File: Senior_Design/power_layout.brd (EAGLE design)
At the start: 108.2 x 35 mm, 103 parts, among them J1 AU-Y1008-2, J1[SIMCARD] 78646-3001, J2 U.FL-R-SMT-1(01), J3 U.FL-R-SMT-1(01), J4[GROVE] 640456-4, T1 BCX70SMD, T2 BCX70SMD, U1 SIM7000E, U2 TUSB2046BVFR, U3 MAX3373EEKA+T, U4 TPS2044BDR, X1 332-04

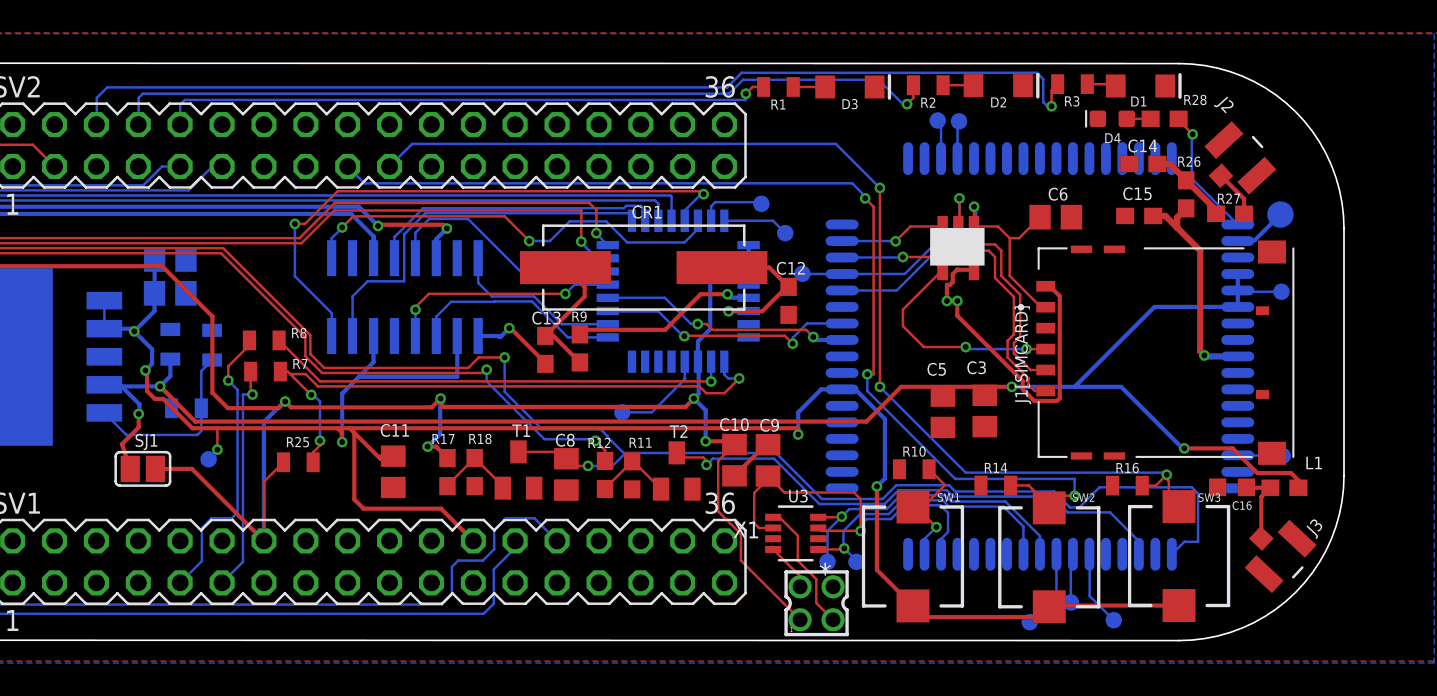
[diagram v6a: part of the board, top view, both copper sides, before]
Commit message: Alpha Order Design Changes
Incorporated all PCB Review design changes
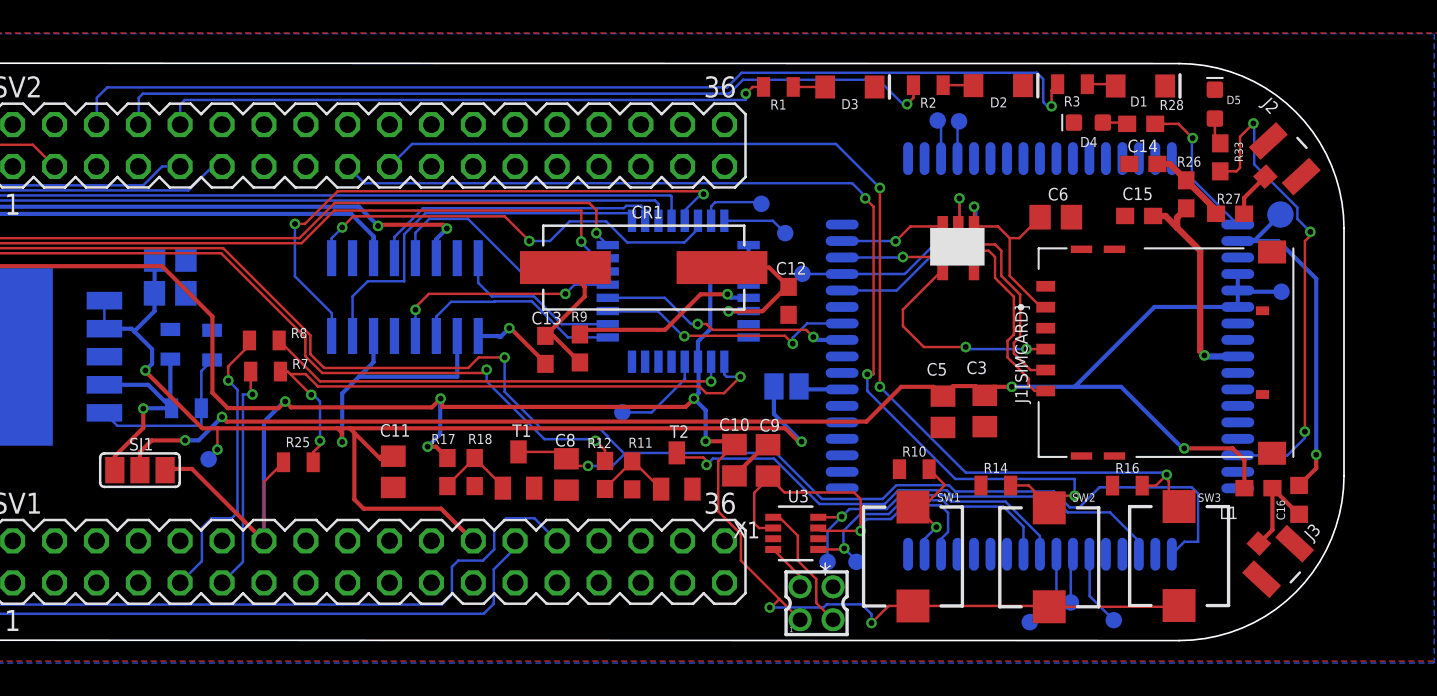
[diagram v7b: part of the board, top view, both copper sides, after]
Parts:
- removed TP20: TPTP10R, testpad:TP10R
- added D5: Yellow, SparkFun-LED:LED-0603
- added R33: 330, SparkFun-Resistors:0603
- added SJ2: (no value), jumper:SJ
- SJ1: device jumper:SJ -> jumper:SJ_2
- moved C16 4.13 mm to (105.4, 8.51), turned to 90 degrees
- moved J2 2.69 mm to (104.6, 29.2)
- moved L1 1.58 mm to (103.0, 9.22), turned to 0 degrees
- moved D4 1.47 mm to (92.7, 31.4)
- moved R28 1.45 mm to (95.9, 31.3)
- moved J3 0.34 mm to (104.2, 4.78)
- moved SJ1 0.19 mm to (35.1, 10.3)
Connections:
- removed net N$15 (its old number): TP2.TP, U1.53
- new net N$36: SJ2.2, U1.24
- new net N$37: D5.A, R33.1
- new net PRE_GPS: C16.2, TP2.TP, U1.53
- new net REGULATED: POWER_SUPPLY.4, R5.2, R6.2, SJ1.3
- net +5V: now also SJ2.1; no longer SW1.P$2, SW2.P$2, SW3.P$2, U1.24
- net 3.3V: now also SW1.P$2, SW2.P$2, SW3.P$2
- net GND: now also D5.C; no longer C16.2
- net MODEM_POWER: no longer POWER_SUPPLY.4, R5.2, R6.2
- net N$33: now also R33.2; no longer TP20.TP
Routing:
- net +5V: track 125.7 -> 91.7 mm, vias 6 -> 4
- net N$33: track 2.74 -> 29.5 mm, vias 0 -> 3
- net 3.3V: track 147.8 -> 174.2 mm, vias 5 -> 7
- net PRE_GPS: track 0.00 -> 21.9 mm, vias 0 -> 1
- net GND: track 35.5 -> 14.9 mm, vias 3 -> 1
- net MODEM_POWER: track 105.5 -> 91.0 mm
- net REGULATED: track 0.00 -> 13.9 mm, vias 0 -> 1
- net N$15 (its old number): track 3.25 -> 0.00 mm
- net N$36: track 0.00 -> 2.69 mm
- net N$37: track 0.00 -> 1.64 mm
- net N$15: track 4.77 -> 5.97 mm
- net N$29: track 7.94 -> 9.05 mm
- net N$3: track 11.1 -> 10.5 mm

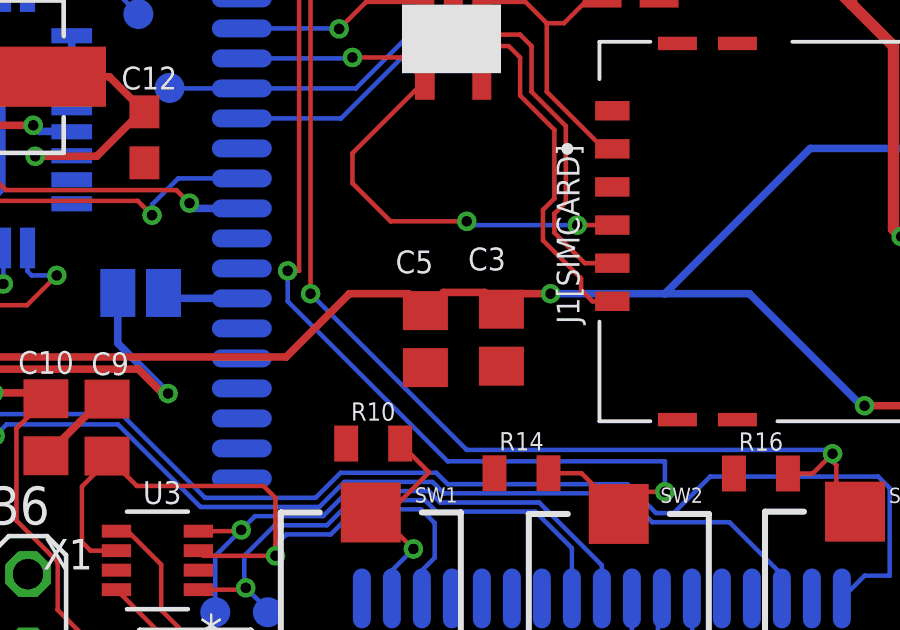
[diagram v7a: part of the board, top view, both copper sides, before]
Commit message: Updated C3 Size and regenerated CAM
Part swap pre-ordering
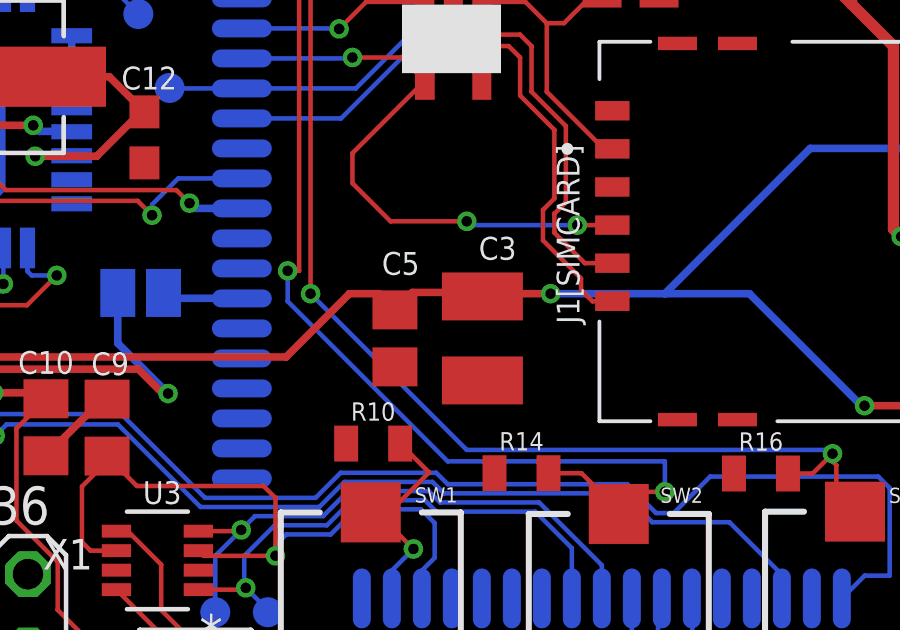
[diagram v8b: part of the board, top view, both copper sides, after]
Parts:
- C3: value (none) -> 330uF; device rcl:C0805 -> rcl:C1210
- C5: value (none) -> 100nF
- R1: value 330 -> 60.4
- R2, R3: value 330 -> 180
- moved C5 1.02 mm to (82.8, 13.9)
- moved C3 0.64 mm to (85.7, 13.9)
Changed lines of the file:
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@@
 <attribute name="VALUE" x="35.311" y="24.0846" size="1.27" layer="28" ratio="10" rot="MR180"/>
 </element>
-<element name="C3" library="rcl" library_urn="urn:adsk.eagle:library:334" package="C0805" package3d_urn="urn:adsk.eagle:package:23617/2" value="" x="86.3734" y="13.9006" smashed="yes" rot="R270">
-<attribute name="NAME" x="85.261" y="16.1424" size="0.762" layer="25" font="vector"/>
-<attribute name="POPULARITY" value="63" x="27.9534" y="-6.4194" size="1.778" layer="27" rot="R270" display="off"/>
-<attribute name="SPICEPREFIX" value="C" x="86.3734" y="13.9006" size="1.778" layer="27" rot="R270" display="off"/>
-<attribute name="VALUE" x="83.3254" y="15.5516" size="1.27" layer="27" ratio="10" rot="R270"/>
+<element name="C3" library="rcl" library_urn="urn:adsk.eagle:library:334" package="C1210" package3d_urn="urn:adsk.eagle:package:23619/2" value="330uF" x="85.7384" y="13.8752" smashed="yes" rot="R270">
+<attribute name="NAME" x="85.6166" y="16.498" size="0.762" layer="25" font="vector"/>
+<attribute name="POPULARITY" value="6" x="27.3184" y="-6.4448" size="1.778" layer="27" rot="R270" display="off"/>
+<attribute name="SPICEPREFIX" value="C" x="85.7384" y="13.8752" size="1.778" layer="27" rot="R270" display="off"/>
 </element>
 <element name="C4" library="rcl" library_urn="urn:adsk.eagle:library:334" package="C0805" package3d_urn="urn:adsk.eagle:package:23617/2" value="" x="36.9678" y="23.0902" smashed="yes" rot="MR180">
@@
 <attribute name="VALUE" x="35.1898" y="25.7572" size="1.27" layer="28" ratio="10" rot="MR180"/>
 </element>
-<element name="C5" library="rcl" library_urn="urn:adsk.eagle:library:334" package="C0805" package3d_urn="urn:adsk.eagle:package:23617/2" value="" x="83.8388" y="13.8536" smashed="yes" rot="R270">
-<attribute name="NAME" x="82.8442" y="16.0462" size="0.762" layer="25" font="vector"/>
-<attribute name="POPULARITY" value="63" x="26.6888" y="-16.6264" size="1.778" layer="27" rot="R270" display="off"/>
-<attribute name="SPICEPREFIX" value="C" x="26.6888" y="-16.6264" size="1.778" layer="27" rot="R270" display="off"/>
-<attribute name="VALUE" x="81.1718" y="15.6316" size="1.27" layer="27" ratio="10" rot="R270"/>
+<element name="C5" library="rcl" library_urn="urn:adsk.eagle:library:334" package="C0805" package3d_urn="urn:adsk.eagle:package:23617/2" value="100nF" x="82.8228" y="13.879" smashed="yes" rot="R270">
+<attribute name="NAME" x="82.387" y="15.9954" size="0.762" layer="25" font="vector"/>
+<attribute name="POPULARITY" value="63" x="25.6728" y="-16.601" size="1.778" layer="27" rot="R270" display="off"/>
+<attribute name="SPICEPREFIX" value="C" x="25.6728" y="-16.601" size="1.778" layer="27" rot="R270" display="off"/>
 </element>
 <element name="POWER_SUPPLY" library="MIC29302WU" package="TO263-5" value="MIC29302WU" x="27.18" y="17.19" smashed="yes" rot="MR270">
@@
 <attribute name="TE_PURCHASE_URL" value="https://www.te.com/usa-en/product-640456-4.html?te_bu=Cor&amp;te_type=disp&amp;te_campaign=seda_glo_cor-seda-global-disp-prtnr-fy19-seda-model-bom-cta_sma-317_1&amp;elqCampaignId=32493" x="20.94" y="30.02" size="1.778" layer="27" display="off"/>
 </element>
-<element name="R1" library="SparkFun-Resistors" library_urn="urn:adsk.eagle:library:532" package="0805" package3d_urn="urn:adsk.eagle:package:39651/1" value="330" x="73.855" y="33.555" smashed="yes" rot="R180">
+<element name="R1" library="SparkFun-Resistors" library_urn="urn:adsk.eagle:library:532" package="0805" package3d_urn="urn:adsk.eagle:package:39651/1" value="60.4" x="73.855" y="33.555" smashed="yes" rot="R180">
 <attribute name="NAME" x="73.855" y="32.793" size="0.6096" layer="25" font="vector" rot="R180" align="bottom-center"/>
 <attribute name="PROD_ID" value=" " x="73.855" y="33.555" size="1.778" layer="27" rot="R180" display="off"/>
 </element>
-<element name="R2" library="SparkFun-Resistors" library_urn="urn:adsk.eagle:library:532" package="0805" package3d_urn="urn:adsk.eagle:package:39651/1" value="330" x="82.945" y="33.665" smashed="yes" rot="R180">
+<element name="R2" library="SparkFun-Resistors" library_urn="urn:adsk.eagle:library:532" package="0805" package3d_urn="urn:adsk.eagle:package:39651/1" value="180" x="82.945" y="33.665" smashed="yes" rot="R180">
 <attribute name="NAME" x="82.945" y="32.903" size="0.6096" layer="25" font="vector" rot="R180" align="bottom-center"/>
 <attribute name="PROD_ID" value=" " x="82.945" y="33.665" size="1.778" layer="27" rot="R180" display="off"/>
 </element>
-<element name="R3" library="SparkFun-Resistors" library_urn="urn:adsk.eagle:library:532" package="0805" package3d_urn="urn:adsk.eagle:package:39651/1" value="330" x="91.695" y="33.725" smashed="yes" rot="R180">
+<element name="R3" library="SparkFun-Resistors" library_urn="urn:adsk.eagle:library:532" package="0805" package3d_urn="urn:adsk.eagle:package:39651/1" value="180" x="91.695" y="33.725" smashed="yes" rot="R180">
 <attribute name="NAME" x="91.6696" y="32.9884" size="0.6096" layer="25" font="vector" rot="R180" align="bottom-center"/>
 <attribute name="PROD_ID" value=" " x="91.695" y="33.725" size="1.778" layer="27" rot="R180" display="off"/>
@@
 <wire x1="104.3686" y1="21.1328" x2="101.847" y2="21.1328" width="0.254" layer="16"/>
 <wire x1="101.847" y1="21.1328" x2="101.72" y2="21.2598" width="0.254" layer="16"/>
-<wire x1="81.3054" y1="15.367" x2="83.2754" y2="15.367" width="0.254" layer="1"/>
-<wire x1="83.2754" y1="15.367" x2="83.8388" y2="14.8036" width="0.254" layer="1"/>
-<wire x1="83.8388" y1="14.8036" x2="84.4446" y2="15.4094" width="0.254" layer="1"/>
-<wire x1="85.8146" y1="15.4094" x2="84.4446" y2="15.4094" width="0.254" layer="1"/>
-<wire x1="85.8146" y1="15.4094" x2="86.3734" y2="14.8506" width="0.254" layer="1"/>
-<wire x1="86.3734" y1="14.8506" x2="86.8898" y2="15.367" width="0.254" layer="1"/>
-<wire x1="86.8898" y1="15.367" x2="88.011" y2="15.367" width="0.254" layer="1"/>
+<wire x1="81.3054" y1="15.367" x2="82.2848" y2="15.367" width="0.254" layer="1"/>
+<wire x1="82.2848" y1="15.367" x2="82.8228" y2="14.829" width="0.254" layer="1"/>
+<wire x1="82.8228" y1="14.829" x2="83.4032" y2="15.4094" width="0.254" layer="1"/>
+<wire x1="85.04914375" y1="15.4094" x2="83.4032" y2="15.4094" width="0.254" layer="1"/>
+<wire x1="85.04914375" y1="15.4094" x2="85.7384" y2="15.2752" width="0.254" layer="1"/>
+<wire x1="85.7384" y1="15.2752" x2="86.4523375" y2="15.367" width="0.254" layer="1"/>
+<wire x1="86.4523375" y1="15.367" x2="88.011" y2="15.367" width="0.254" layer="1"/>
 </signal>
 <signal name="N$29">
